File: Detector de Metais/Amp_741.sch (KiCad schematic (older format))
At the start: 15 parts, among them Q1 BC807-40, Q2 BF245A, U4 LM741

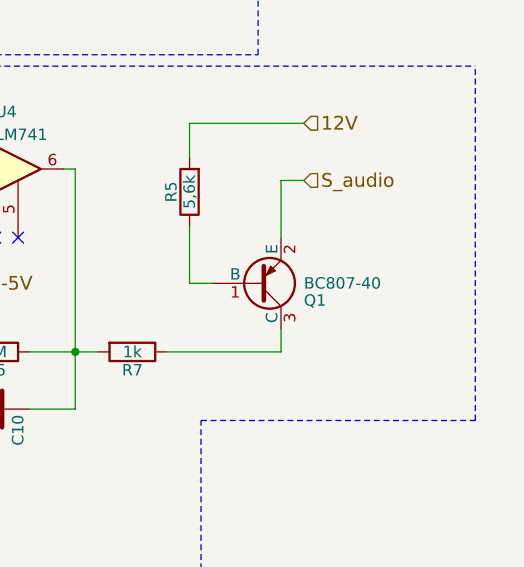
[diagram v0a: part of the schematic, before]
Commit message: Atualizando simbolos e criando footprint
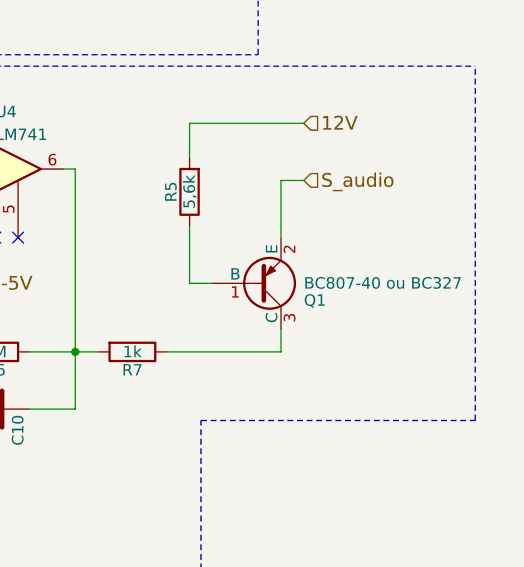
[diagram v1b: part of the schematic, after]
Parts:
- C10: footprint (none) -> Capacitor_THT:C_Disc_D6.0mm_W4.4mm_P5.00mm
- POT1, POT2: footprint (none) -> Potentiometer_THT:Potentiometer_Vishay_148-149_Single_Horizontal
- PTR1: footprint (none) -> Potentiometer_THT:Potentiometer_ACP_CA9-H3,8_Horizontal
- Q1: value BC807-40 -> BC807-40 ou BC327
- R10: footprint (none) -> Resistor_SMD:R_0805_2012Metric_Pad1.15x1.40mm_HandSolder
- R3: footprint (none) -> Resistor_THT:R_Axial_DIN0204_L3.6mm_D1.6mm_P1.90mm_Vertical
- U4: footprint (none) -> Package_DIP:DIP-8_W7.62mm_LongPads
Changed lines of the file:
@@
 F 0 "U4" H 5900 3800 50  0000 L CNN
 F 1 "LM741" H 5900 3700 50  0000 L CNN
-F 2 "" H 5950 3600 50  0001 C CNN
+F 2 "Package_DIP:DIP-8_W7.62mm_LongPads" H 5950 3600 50  0001 C CNN
 F 3 "" H 6050 3700 50  0001 C CNN
 	1    5900 3550
@@
 F 0 "C10" H 5925 4700 50  0000 L CNN
 F 1 "220nF" V 5950 4300 50  0000 L CNN
-F 2 "" H 5938 4450 50  0001 C CNN
+F 2 "Capacitor_THT:C_Disc_D6.0mm_W4.4mm_P5.00mm" H 5938 4450 50  0001 C CNN
 F 3 "" H 5900 4600 50  0001 C CNN
 	1    5900 4600
@@
 P 7050 4050
 F 0 "Q1" H 7250 4125 50  0000 L CNN
-F 1 "BC807-40" H 7250 4050 50  0000 L CNN
+F 1 "BC807-40 ou BC327" H 7250 4050 50  0000 L CNN
 F 2 "TO_SOT_Packages_SMD:SOT-23" H 7250 3975 50  0001 L CIN
 F 3 "" H 7050 4050 50  0001 L CNN
@@
 F 0 "POT1" V 5225 2300 50  0000 C CNN
 F 1 "10k" V 5300 2300 50  0000 C CNN
-F 2 "" H 5400 2300 50  0001 C CNN
+F 2 "Potentiometer_THT:Potentiometer_Vishay_148-149_Single_Horizontal" H 5400 2300 50  0001 C CNN
 F 3 "" H 5400 2300 50  0001 C CNN
 	1    5400 2300
@@
 F 0 "POT2" V 5875 2300 50  0000 C CNN
 F 1 "2,2k" V 5950 2300 50  0000 C CNN
-F 2 "" H 6050 2300 50  0001 C CNN
+F 2 "Potentiometer_THT:Potentiometer_Vishay_148-149_Single_Horizontal" H 6050 2300 50  0001 C CNN
 F 3 "" H 6050 2300 50  0001 C CNN
 	1    6050 2300
@@
 F 1 "BF245A" H 5500 5100 50  0000 L CNN
 F 2 "TO_SOT_Packages_THT:TO-92_Molded_Narrow" H 5500 5025 50  0001 L CIN
-F 3 "" H 5300 5050 50  0001 L CNN
+F 3 "Falta" H 5300 5050 50  0001 L CNN
 	1    5300 5100
 	1    0    0    -1
@@
 F 0 "R10" V 5480 5550 50  0000 C CNN
 F 1 "10k" V 5400 5550 50  0000 C CNN
-F 2 "" V 5330 5550 50  0001 C CNN
+F 2 "Resistor_SMD:R_0805_2012Metric_Pad1.15x1.40mm_HandSolder" V 5330 5550 50  0001 C CNN
 F 3 "" H 5400 5550 50  0001 C CNN
 	1    5400 5550
@@
 F 0 "R3" V 5030 2050 50  0000 C CNN
 F 1 "36k" V 4950 2050 50  0000 C CNN
-F 2 "" V 4880 2050 50  0001 C CNN
-F 3 "" H 4950 2050 50  0001 C CNN
+F 2 "Resistor_THT:R_Axial_DIN0204_L3.6mm_D1.6mm_P1.90mm_Vertical" V 4880 2050 50  0001 C CNN
+F 3 "Falta" H 4950 2050 50  0001 C CNN
 	1    4950 2050
 	-1   0    0    1
@@
 F 0 "PTR1" V 6375 2300 50  0000 C CNN
 F 1 "220k" V 6450 2300 50  0000 C CNN
-F 2 "" H 6550 2300 50  0001 C CNN
+F 2 "Potentiometer_THT:Potentiometer_ACP_CA9-H3,8_Horizontal" H 6550 2300 50  0001 C CNN
 F 3 "" H 6550 2300 50  0001 C CNN
 	1    6550 2300

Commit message: Desenhando fonte
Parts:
- Q1: footprint TO_SOT_Packages_SMD:SOT-23 -> Package_TO_SOT_THT:TO-92
- Q2: footprint TO_SOT_Packages_THT:TO-92_Molded_Narrow -> Package_TO_SOT_THT:TO-92
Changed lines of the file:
@@
 F 0 "Q1" H 7250 4125 50  0000 L CNN
 F 1 "BC807-40 ou BC327" H 7250 4050 50  0000 L CNN
-F 2 "TO_SOT_Packages_SMD:SOT-23" H 7250 3975 50  0001 L CIN
+F 2 "Package_TO_SOT_THT:TO-92" H 7250 3975 50  0001 L CIN
 F 3 "" H 7050 4050 50  0001 L CNN
 	1    7050 4050
@@
 F 0 "Q2" H 5500 5175 50  0000 L CNN
 F 1 "BF245A" H 5500 5100 50  0000 L CNN
-F 2 "TO_SOT_Packages_THT:TO-92_Molded_Narrow" H 5500 5025 50  0001 L CIN
+F 2 "Package_TO_SOT_THT:TO-92" H 5500 5025 50  0001 L CIN
 F 3 "Falta" H 5300 5050 50  0001 L CNN
 	1    5300 5100
